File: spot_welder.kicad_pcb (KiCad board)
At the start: 2 copper layers, 90.8 x 61.6 mm, 20 parts, among them J1 Conn_01x02_Female, J2 Conn_01x02_Female, Q1 BSR20, Q2 BSR20, Q3 BSR20, SW1 Rotary_Encoder_Switch, U1 Stm8S103F6_module, U2 KCSA02-123, U3 KCSA02-123, U4 KCSA02-123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

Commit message: mounting holes added
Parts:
- added H1: MountingHole, MountingHole:MountingHole_3.2mm_M3_DIN965_Pad, F.Cu at (97.2, 126.4)
- added H2: MountingHole, MountingHole:MountingHole_3.2mm_M3_DIN965_Pad, F.Cu at (97.2, 74.9)
- added H4: MountingHole, MountingHole:MountingHole_3.2mm_M3_DIN965_Pad, F.Cu at (177.8, 101.6)
- added J3: Supply, Connector_Phoenix_GMSTB:PhoenixContact_GMSTBVA_2,5_2-G-7,62_1x02_P7.62mm_Vertical, F.Cu at (101.6, 116.2)
- moved C1 2.92 mm to (149.5, 116.2)
- moved R7 1.14 mm to (153.0, 114.3)
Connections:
- U1 pad 18: (no net) -> /swim
- U1 pad 2: (no net) -> Net-(U1-Pad2)
- U1 pad 4: (no net) -> Net-(U1-Pad4)
- U1 pad 8: +3V3 -> Net-(J3-Pad2)
- U1 pad 9: (no net) -> +3V3
- U2 pad 8: (no net) -> Net-(U2-Pad8)
- U3 pad 8: (no net) -> Net-(U3-Pad8)
- U4 pad 8: (no net) -> Net-(U4-Pad8)
- U5 pad 3: (no net) -> Net-(U5-Pad3)
- U5 pad 5: (no net) -> Net-(U5-Pad5)
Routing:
- net Net-(J3-Pad2): track 0.00 -> 23.5 mm
- net GND: track 42.7 -> 60.3 mm
- net Net-(C1-Pad2): track 50.2 -> 44.8 mm
- net /c: track 126.6 -> 129.7 mm
- net +3V3: track 122.4 -> 120.0 mm
- net /OPTO: track 27.5 -> 29.4 mm
- net Net-(D1-Pad2): track 31.3 -> 30.5 mm

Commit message: Add segment resistors
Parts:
- added R10: 220, Resistor_SMD:R_0805_2012Metric_Pad1.15x1.40mm_HandSolder, B.Cu at (132.1, 85.1)
- added R11: 220, Resistor_SMD:R_0805_2012Metric_Pad1.15x1.40mm_HandSolder, B.Cu at (132.1, 96.5)
- added R12: 220, Resistor_SMD:R_0805_2012Metric_Pad1.15x1.40mm_HandSolder, B.Cu at (124.5, 80.0)
- added R13: 220, Resistor_SMD:R_0805_2012Metric_Pad1.15x1.40mm_HandSolder, B.Cu at (132.1, 87.6)
- added R14: 220, Resistor_SMD:R_0805_2012Metric_Pad1.15x1.40mm_HandSolder, B.Cu at (132.7, 100.3)
- added R8: 220, Resistor_SMD:R_0805_2012Metric_Pad1.15x1.40mm_HandSolder, B.Cu at (117.5, 77.5)
- added R9: 220, Resistor_SMD:R_0805_2012Metric_Pad1.15x1.40mm_HandSolder, B.Cu at (132.1, 77.5)
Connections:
- U1 pad 1: /e -> Net-(R8-Pad2)
- U1 pad 11: /b -> Net-(R14-Pad1)
- U1 pad 12: /a -> Net-(R11-Pad1)
- U1 pad 16: /f -> Net-(R13-Pad1)
- U1 pad 17: /g -> Net-(R10-Pad1)
- U1 pad 18: /swim -> (no net)
- U1 pad 19: /c -> Net-(R12-Pad1)
- U1 pad 2: Net-(U1-Pad2) -> (no net)
- U1 pad 20: /d -> Net-(R9-Pad1)
- U1 pad 4: Net-(U1-Pad4) -> (no net)
- U2 pad 8: Net-(U2-Pad8) -> (no net)
- U3 pad 8: Net-(U3-Pad8) -> (no net)
- U4 pad 8: Net-(U4-Pad8) -> (no net)
- U5 pad 3: Net-(U5-Pad3) -> (no net)
- U5 pad 5: Net-(U5-Pad5) -> (no net)
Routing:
- net /e: track 137.9 -> 132.5 mm
- net /f: track 53.8 -> 49.2 mm
- net /g: track 53.6 -> 49.1 mm
- net Net-(R11-Pad1): track 0.00 -> 3.91 mm
- net /a: track 59.0 -> 55.1 mm
- net /d: track 109.3 -> 105.5 mm
- net Net-(R8-Pad2): track 0.00 -> 3.42 mm
- net Net-(R14-Pad1): track 0.00 -> 3.42 mm
- net Net-(R12-Pad1): track 0.00 -> 2.79 mm
- net Net-(R9-Pad1): track 0.00 -> 2.78 mm
- net Net-(R13-Pad1): track 0.00 -> 2.78 mm
- net Net-(R10-Pad1): track 0.00 -> 2.78 mm
- net /b: track 66.1 -> 64.0 mm
- net /c: track 129.7 -> 127.6 mm

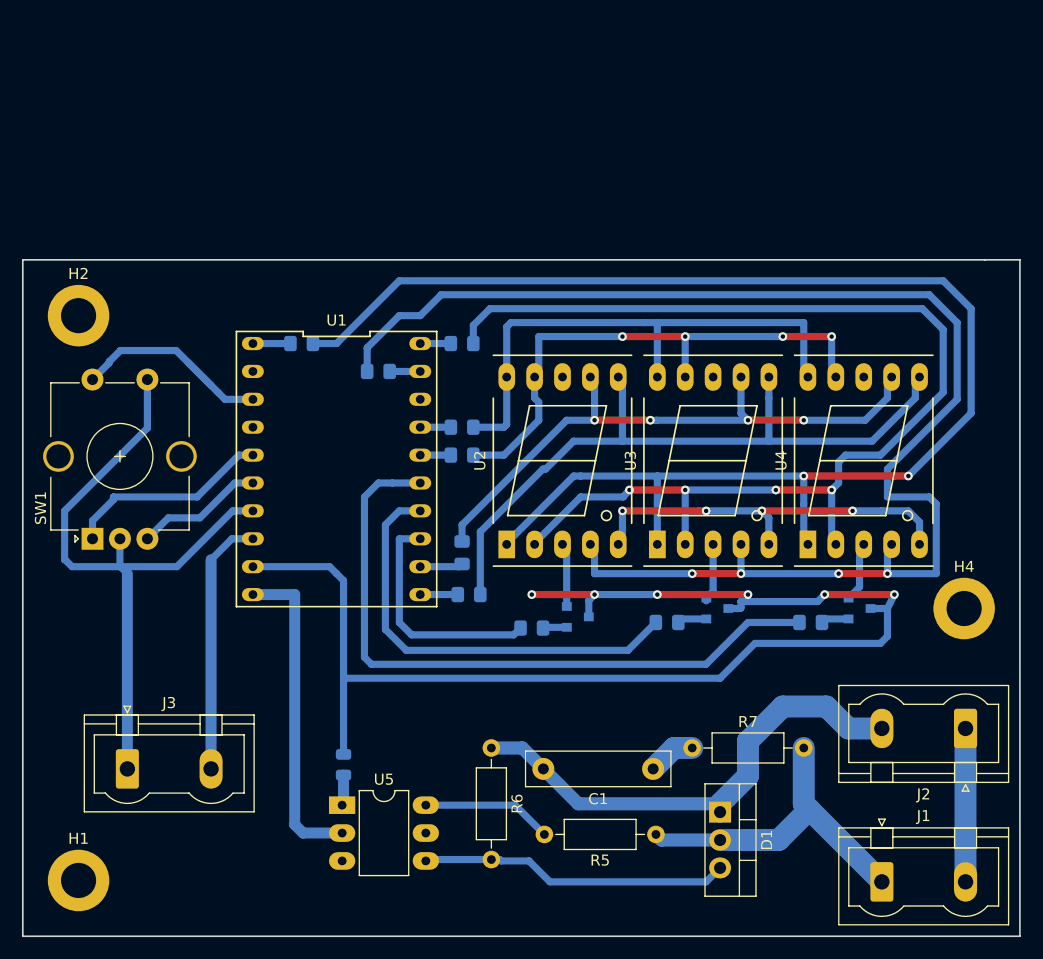
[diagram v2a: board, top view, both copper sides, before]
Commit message: encoder moved to right of display
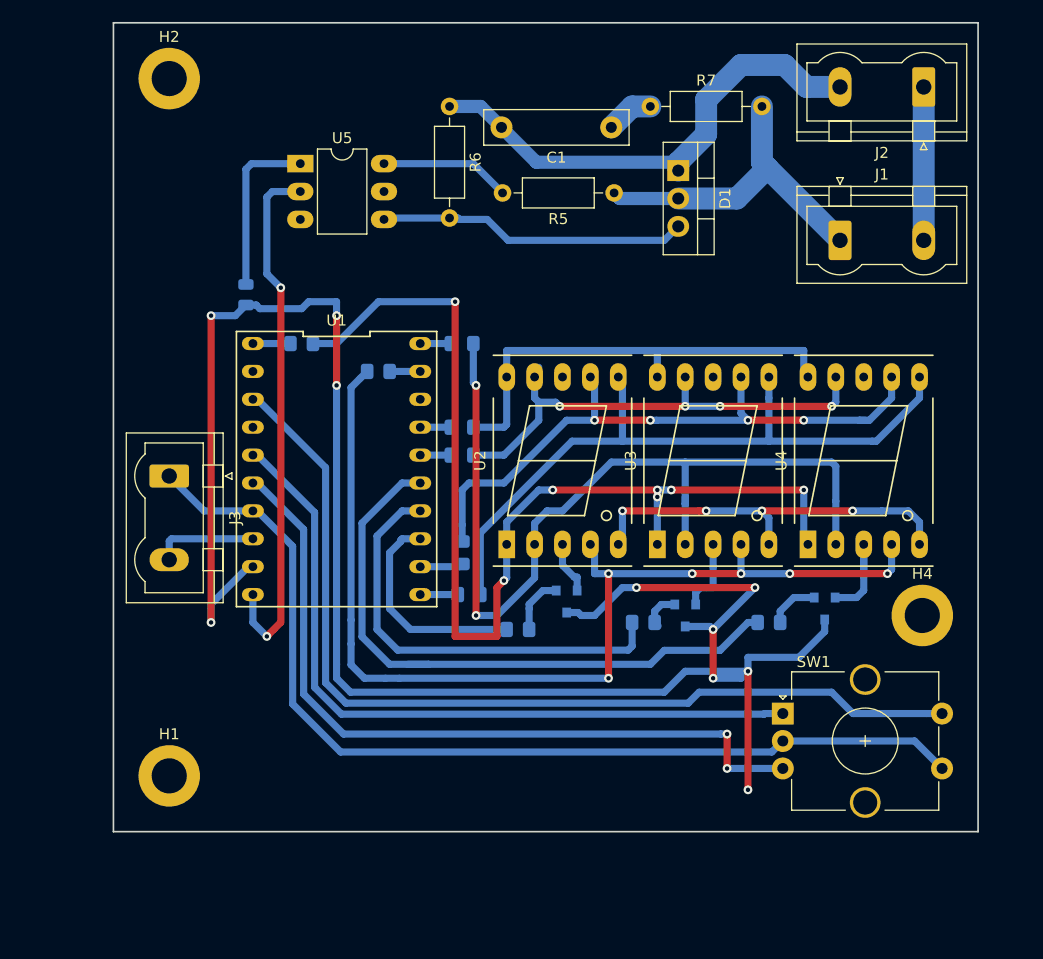
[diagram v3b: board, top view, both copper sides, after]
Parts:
- moved SW1 64.8 mm to (161.3, 111.2), turned to 0 degrees
- moved J2 58.5 mm to (174.1, 54.1)
- moved R5 58.5 mm to (145.9, 63.8)
- moved C1 58.5 mm to (145.7, 57.8)
- moved U5 58.5 mm to (117.3, 61.1)
- moved D1 58.5 mm to (151.8, 61.7)
- moved R6 58.5 mm to (130.9, 55.9)
- moved R7 58.5 mm to (149.2, 55.9)
- moved J1 58.5 mm to (166.5, 68.1)
- moved R4 43.7 mm to (112.4, 73.0), turned to 90 degrees
- moved J3 26.9 mm to (105.4, 89.5), turned to 270 degrees
- moved H2 23.1 mm to (105.4, 53.3)
- moved H1 12.6 mm to (105.4, 116.8)
- moved H4 3.86 mm to (174.0, 102.2)
- moved R3 3.81 mm to (160.0, 102.9)
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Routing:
- net /SW: track 20.5 -> 86.9 mm
- net /EN_B: track 11.7 -> 69.7 mm, vias 0 -> 2
- net +3V3: track 120.0 -> 175.5 mm, vias 6 -> 10
- net /EN_A: track 18.9 -> 67.4 mm
- net /e: track 132.5 -> 98.4 mm, vias 2 -> 7
- net /c: track 127.6 -> 95.6 mm, vias 4 -> 6
- net GND: track 60.3 -> 90.7 mm
- net /d: track 105.5 -> 82.2 mm, vias 4 -> 2
- net /OPTO: track 29.4 -> 48.7 mm, vias 0 -> 2
- net Net-(J3-Pad2): track 23.5 -> 9.40 mm
- net Net-(R4-Pad2): track 2.80 -> 16.4 mm
- net /g: track 49.1 -> 41.8 mm
- net /f: track 49.2 -> 44.7 mm
- net Net-(Q3-Pad2): track 5.64 -> 9.99 mm
- net Net-(R3-Pad1): track 61.7 -> 57.7 mm
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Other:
- board size 90.8 x 61.6 mm -> 78.7 x 73.7 mm
- net class Default: clearance 0.2 -> 0.35
- rule trace_clearance: 0.2 -> 0.35

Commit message: 3x7seg LED module
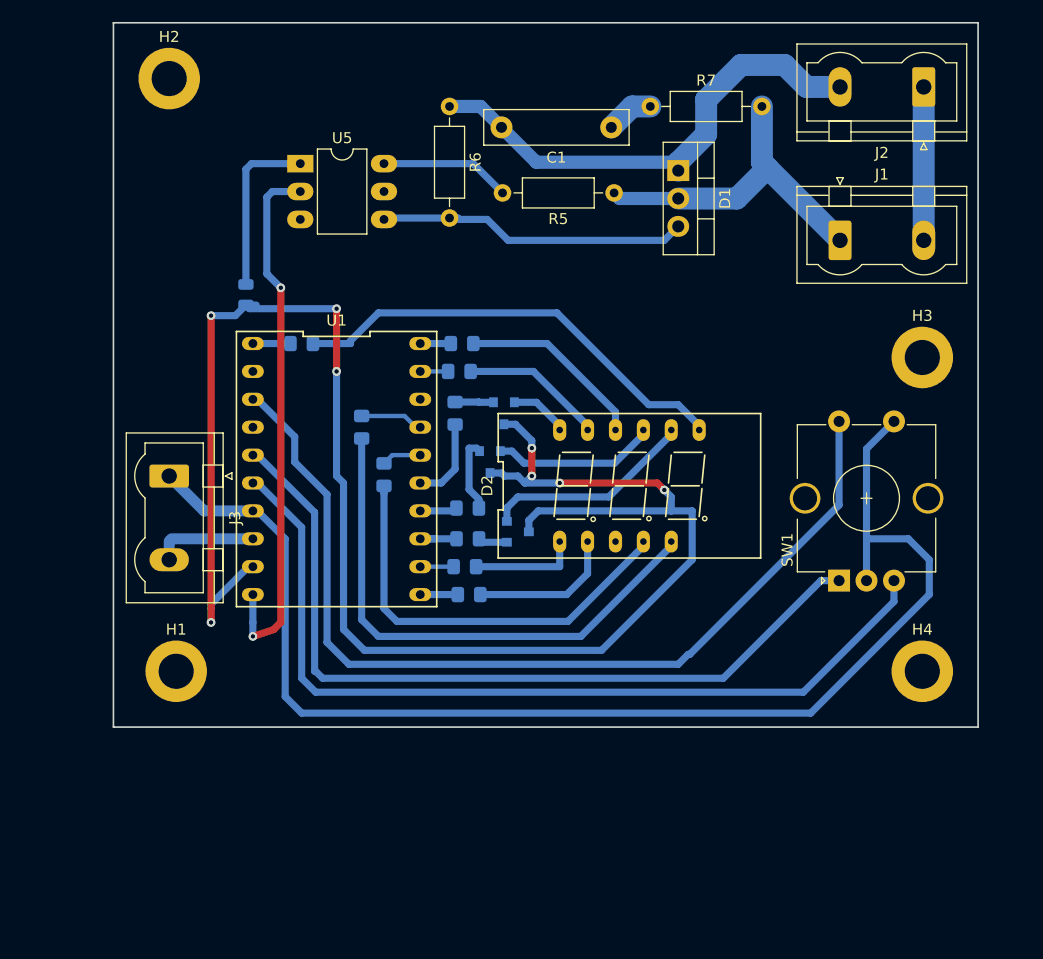
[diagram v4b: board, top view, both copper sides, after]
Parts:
- removed U2, U3, U4: KCSA02-123, Display_7Segment:7SegmentLED_LTS6760_LTS6780
- added D2: SM410363, ebay_modules:SM410363, F.Cu at (147.3, 90.4)
- added H3: MountingHole, MountingHole:MountingHole_3.2mm_M3_DIN965_Pad, F.Cu at (174.0, 78.7)
- moved Q3 28.8 mm to (137.2, 94.6), turned to 0 degrees
- moved R3 28.5 mm to (132.6, 95.2)
- moved Q2 22.6 mm to (134.6, 88.3)
- moved R1 20.5 mm to (131.4, 83.8), turned to 90 degrees
- moved R2 19.1 mm to (132.6, 92.5)
- moved Q1 18.1 mm to (135.9, 83.8)
- moved SW1 13.1 mm to (166.4, 99.1), turned to 90 degrees
- moved H1 9.55 mm to (106.0, 107.3)
- moved R10 9.14 mm to (122.9, 85.1), turned to 270 degrees
- moved R12 7.38 mm to (131.8, 80.0), turned to 0 degrees
- moved R13 7.33 mm to (125.0, 89.4), turned to 270 degrees
- moved H4 5.08 mm to (174.0, 107.3)
- moved R11 1.30 mm to (132.3, 97.8), turned to 0 degrees
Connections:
- R11 pad 2: /a -> /e
- R12 pad 2: /c -> /a
- R13 pad 2: /f -> /c
- R14 pad 2: /b -> /d
- R8 pad 1: /e -> /b
- R9 pad 2: /d -> /f
- U1 pad 13: Net-(R1-Pad1) -> Net-(R3-Pad1)
- U1 pad 15: Net-(R3-Pad1) -> Net-(R1-Pad1)
- U1 pad 18: (no net) -> /swim
- U1 pad 2: (no net) -> Net-(U1-Pad2)
- U1 pad 4: (no net) -> Net-(U1-Pad4)
- U5 pad 3: (no net) -> Net-(U5-Pad3)
- U5 pad 5: (no net) -> Net-(U5-Pad5)
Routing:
- net /e: track 98.4 -> 9.90 mm, vias 7 -> 0
- net /d: track 82.2 -> 13.5 mm, vias 2 -> 0
- net /c: track 95.6 -> 38.5 mm, vias 6 -> 0
- net Net-(R3-Pad1): track 57.7 -> 4.70 mm
- net /a: track 57.8 -> 13.1 mm, vias 4 -> 0
- net Net-(R2-Pad2): track 39.7 -> 3.40 mm
- net /dp: track 35.9 -> 0.00 mm, vias 4 -> 0
- net /f: track 44.7 -> 17.2 mm, vias 4 -> 0
- net GND: track 90.7 -> 116.3 mm
- net /b: track 64.3 -> 41.1 mm
- net +3V3: track 175.5 -> 159.9 mm, vias 10 -> 8
- net Net-(R1-Pad1): track 19.9 -> 7.76 mm
- net /EN_B: track 69.7 -> 79.6 mm, vias 2 -> 0
- net Net-(D2-Pad7): track 9.99 -> 19.4 mm
- net Net-(D2-Pad8): track 6.81 -> 15.0 mm
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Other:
- board size 78.7 x 73.7 mm -> 78.7 x 64.1 mm

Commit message: HV part at bottom of PCB
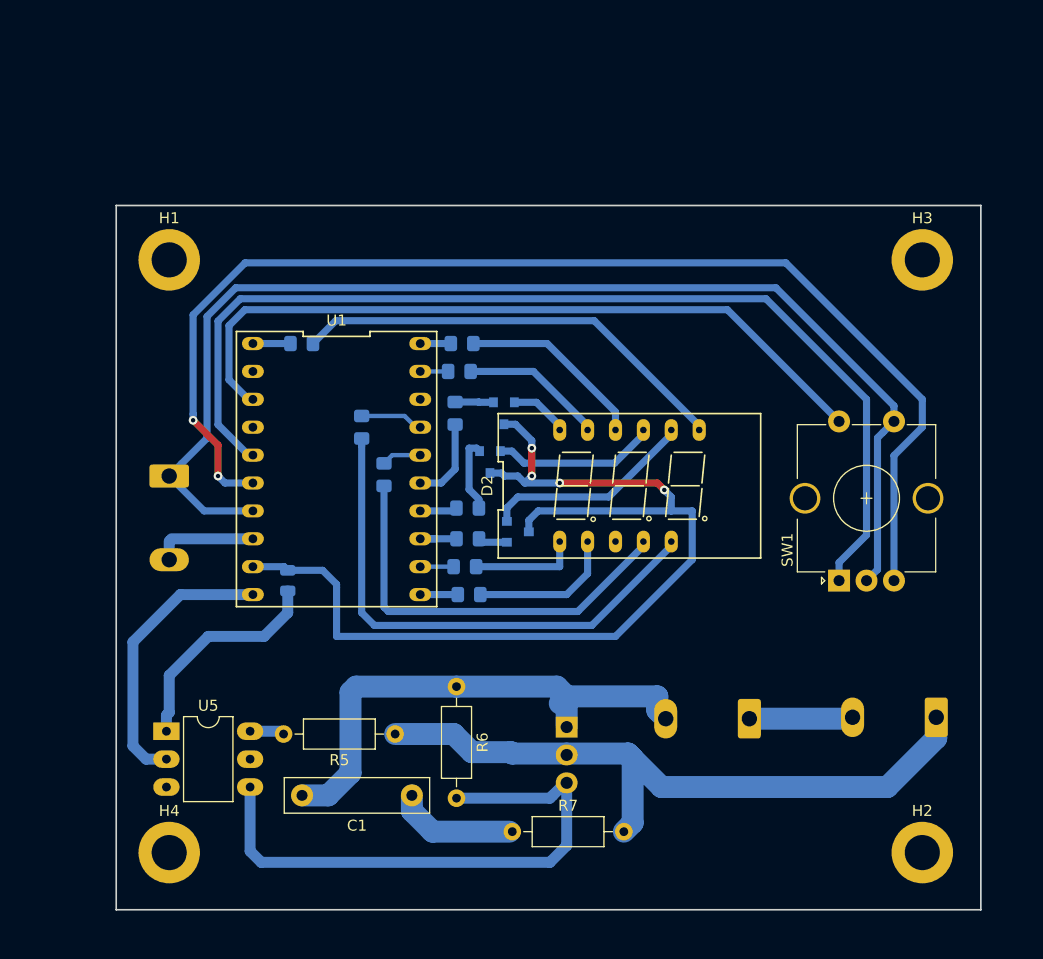
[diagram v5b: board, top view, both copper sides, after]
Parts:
- D1, J1, J2, J3: moved to B.Cu
- moved H2 98.3 mm to (174.0, 123.8)
- moved H4 70.5 mm to (105.4, 123.8)
- moved R7 67.2 mm to (136.7, 121.9)
- moved C1 63.5 mm to (127.5, 118.6)
- moved J2 59.7 mm to (158.2, 111.6)
- moved R5 53.2 mm to (126.0, 113.0)
- moved U5 53.1 mm to (105.2, 112.8)
- moved R6 52.8 mm to (131.6, 108.7)
- moved D1 51.7 mm to (141.6, 112.4)
- moved J1 44.3 mm to (175.3, 111.5), turned to 180 degrees
- moved H1 37.5 mm to (105.4, 69.8)
- moved R4 26.3 mm to (116.2, 99.1), turned to 270 degrees
- moved H3 8.89 mm to (174.0, 69.8)
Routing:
- net +3V3: track 159.9 -> 95.4 mm, vias 8 -> 4
- net Net-(D1-Pad2): track 30.5 -> 63.4 mm
- net /EN_B: track 79.6 -> 110.5 mm, vias 0 -> 2
- net Net-(D1-Pad3): track 28.2 -> 52.2 mm
- net /OPTO: track 49.2 -> 25.7 mm, vias 2 -> 0
- net /EN_A: track 74.0 -> 95.0 mm
- net /SW: track 86.2 -> 68.2 mm
- net Net-(R5-Pad2): track 11.9 -> 3.15 mm
- net Net-(C1-Pad1): track 4.35 -> 11.1 mm
- net GND: track 116.3 -> 109.9 mm
- net Net-(J1-Pad2): track 14.0 -> 9.45 mm
- net Net-(R4-Pad2): track 16.4 -> 20.3 mm
- net Net-(C1-Pad2): track 44.8 -> 47.1 mm
- net /g: track 49.1 -> 47.9 mm
- net /c: track 38.5 -> 37.7 mm
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
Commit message: clearances increased, vias enlarged
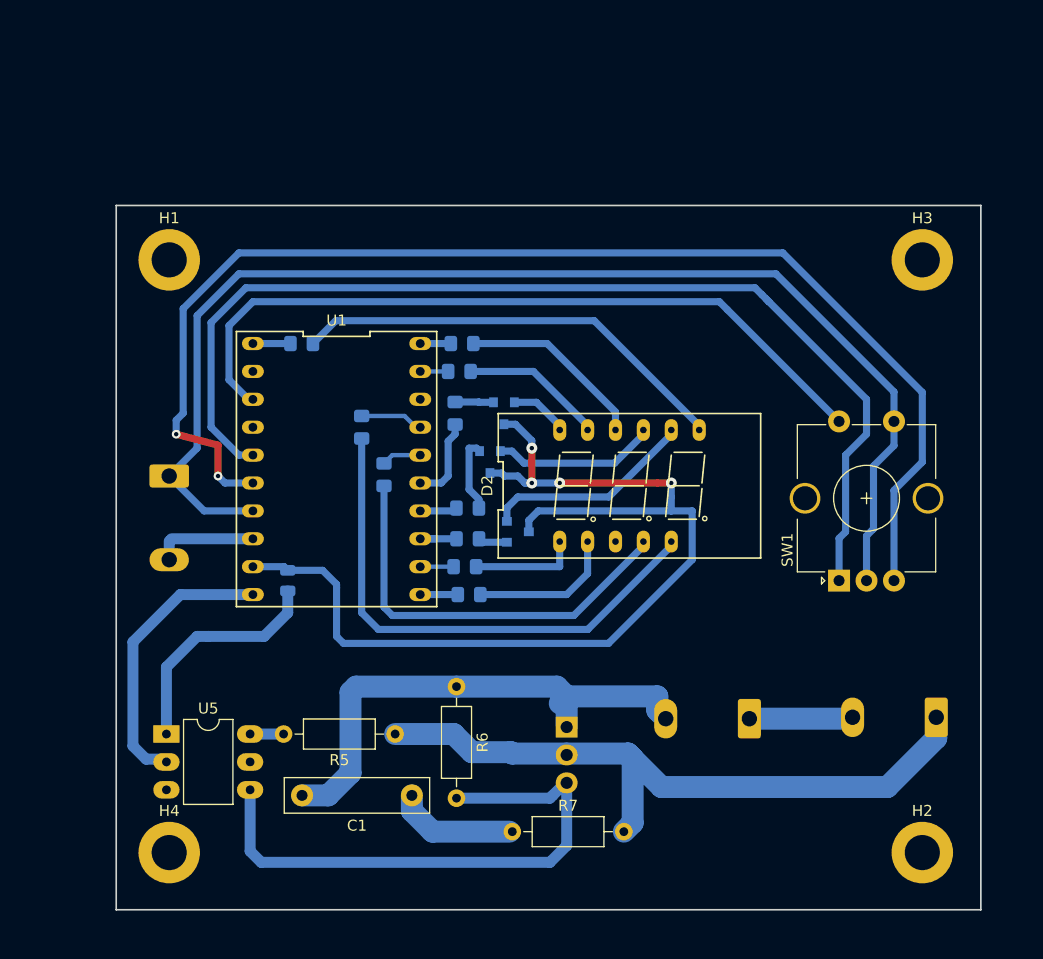
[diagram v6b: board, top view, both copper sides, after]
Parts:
- Q1, Q2, Q3: value BSR20 -> BC807
- moved U5 0.25 mm to (105.2, 113.0)
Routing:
- net /EN_B: track 110.5 -> 115.2 mm
- net /EN_A: track 95.0 -> 97.5 mm
- net GND: track 109.9 -> 112.3 mm
- net +3V3: track 95.4 -> 97.0 mm
- net Net-(R4-Pad2): track 20.3 -> 21.2 mm
- net /SW: track 68.2 -> 68.8 mm
